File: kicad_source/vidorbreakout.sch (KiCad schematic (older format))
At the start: 12 parts, among them CN1 TE_2041119-2, CN2 CONN_01X18, CN3 CONN_01X18

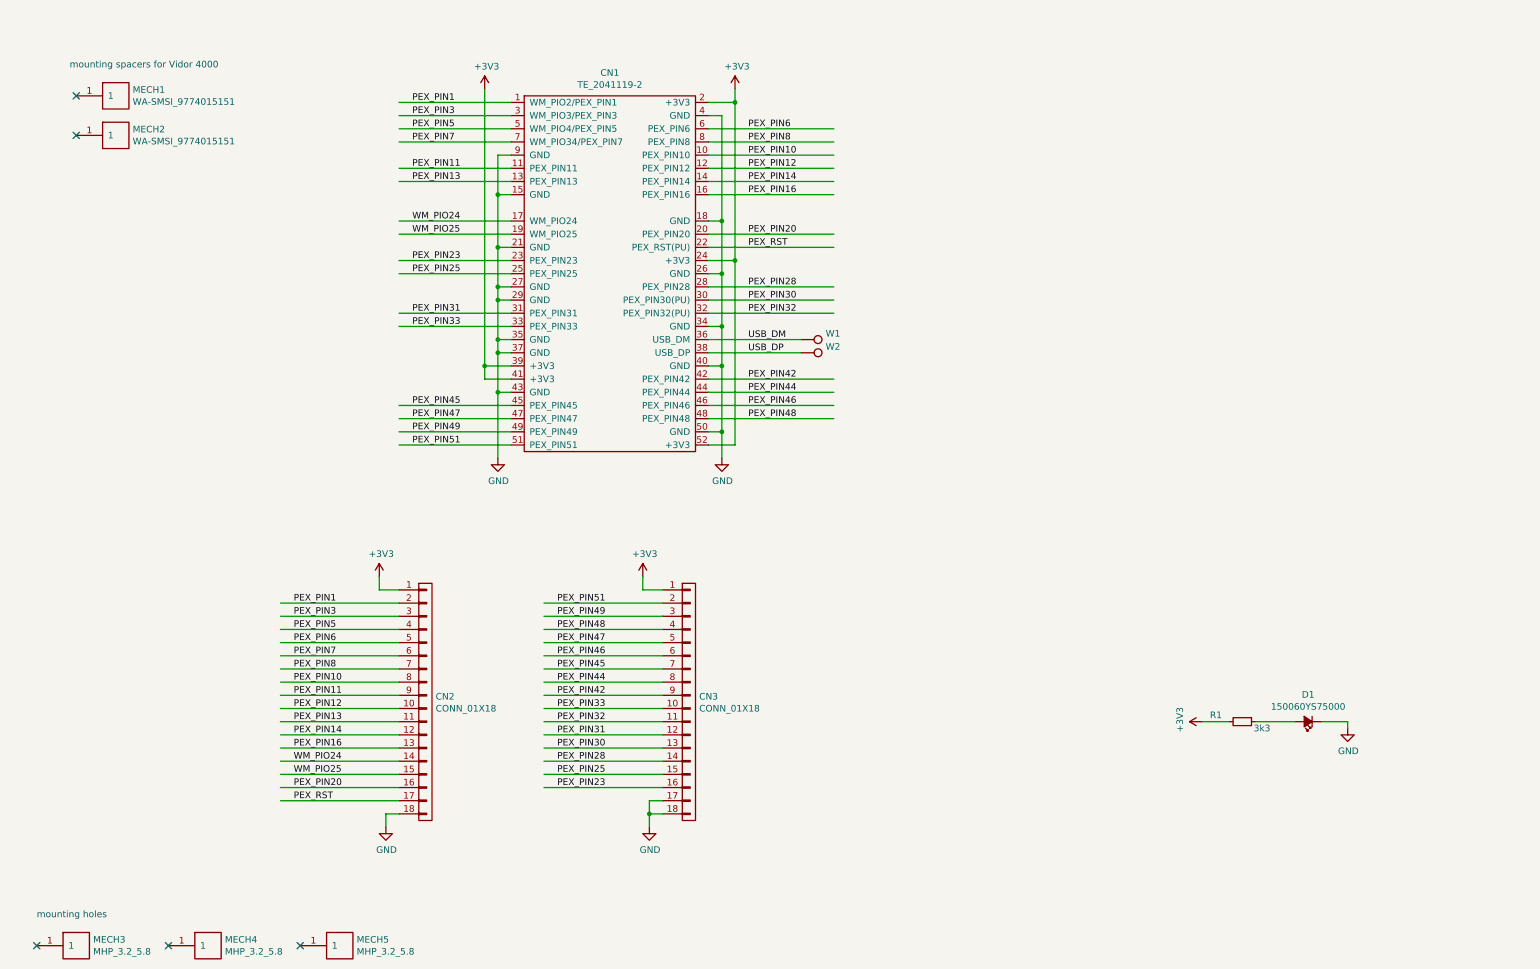
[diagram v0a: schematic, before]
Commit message: added license information in schematic and layout, improved silkscreen
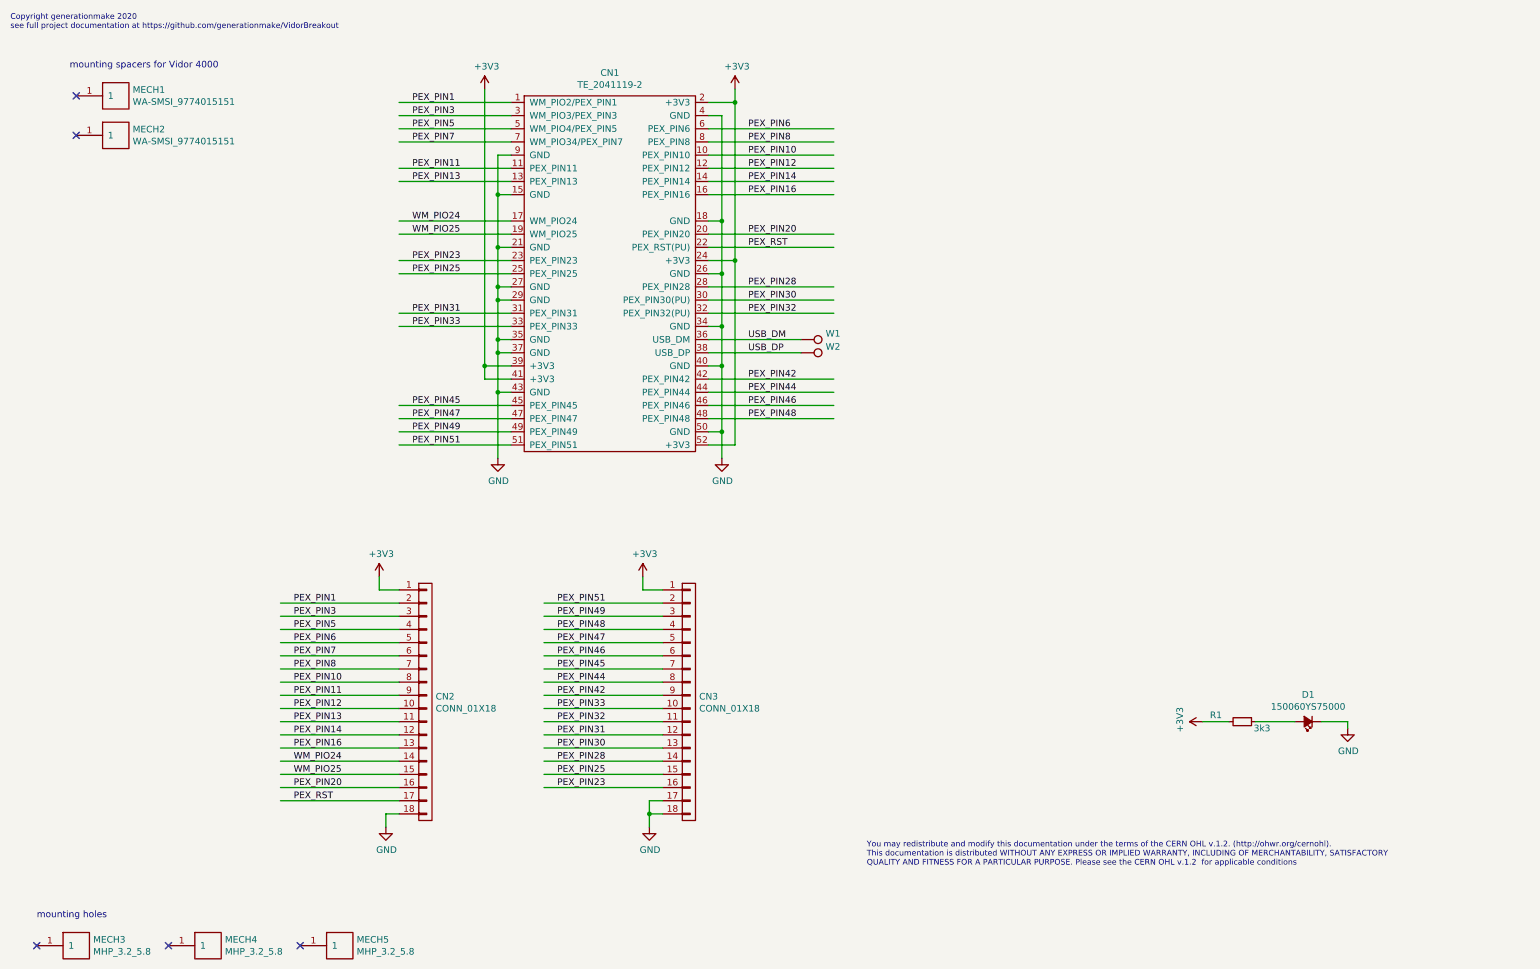
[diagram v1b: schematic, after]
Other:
- note added: "Copyright generationmake 2020\nsee full project documentation at https://github.com/generationmake/VidorBreakout"
- note added: "You may redistribute and modify this documentation under the terms of the CERN OHL v.1.2. (http://ohwr.org/cernohl). \nThis documentation is distributed WITHOUT ANY EXPRESS OR IMPLIED WARRANTY, INCLUDING OF MERCHANTABILITY, SATISFACTORY \nQUALITY AND FITNESS FOR A PARTICULAR PURPOSE. Please see the CERN OHL v.1.2 for applicable conditions"
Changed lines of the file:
@@
 Comment2 ""
 Comment3 ""
-Comment4 ""
+Comment4 "This documentation describes Open Hardware and is licensed under the CERN OHL v. 1.2."
 $EndDescr
 $Comp
@@
 	5350 6500 5350 6600
 Connection ~ 5350 6600
+Text Notes 7000 7000 0    43   ~ 0
+You may redistribute and modify this documentation under the terms of the CERN OHL v.1.2. (http://ohwr.org/cernohl). \nThis documentation is distributed WITHOUT ANY EXPRESS OR IMPLIED WARRANTY, INCLUDING OF MERCHANTABILITY, SATISFACTORY \nQUALITY AND FITNESS FOR A PARTICULAR PURPOSE. Please see the CERN OHL v.1.2  for applicable conditions
+Text Notes 500  650  0    43   ~ 0
+Copyright generationmake 2020\nsee full project documentation at https://github.com/generationmake/VidorBreakout
 $EndSCHEMATC
